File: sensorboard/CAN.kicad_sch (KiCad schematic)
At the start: 14 parts

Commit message: schemtiac update
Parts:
- JP11: renamed from JP?; footprint (none) -> Jumper:SolderJumper-2_P1.3mm_Open_RoundedPad1.0x1.5mm
- gave numbers to parts that had none: 13
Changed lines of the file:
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@@
   (symbol (lib_id "power:GND") (at 133.35 99.06 0) (unit 1)
     (in_bom yes) (on_board yes)
-    (property "Reference" "#PWR?" (id 0) (at 133.35 105.41 0)
+    (property "Reference" "#PWR0156" (id 0) (at 133.35 105.41 0)
       (effects (font (size 1.27 1.27)) hide)
     )
@@
   (symbol (lib_id "power:GND") (at 133.35 85.09 0) (unit 1)
     (in_bom yes) (on_board yes) (fields_autoplaced)
-    (property "Reference" "#PWR?" (id 0) (at 133.35 91.44 0)
+    (property "Reference" "#PWR0155" (id 0) (at 133.35 91.44 0)
       (effects (font (size 1.27 1.27)) hide)
     )
@@
   (symbol (lib_id "Device:C_Small") (at 87.63 83.82 180) (unit 1)
     (in_bom yes) (on_board yes)
-    (property "Reference" "C?" (id 0) (at 88.9 77.47 0)
+    (property "Reference" "C31" (id 0) (at 88.9 77.47 0)
       (effects (font (size 1.27 1.27)) (justify right))
     )
@@
   (symbol (lib_id "Device:C_Small") (at 133.35 96.52 180) (unit 1)
     (in_bom yes) (on_board yes)
-    (property "Reference" "C?" (id 0) (at 135.89 96.52 0)
+    (property "Reference" "C75" (id 0) (at 135.89 96.52 0)
       (effects (font (size 1.27 1.27)) (justify right))
     )
@@
   (symbol (lib_id "Interface_CAN_LIN:SN65HVD230") (at 104.14 83.82 0) (unit 1)
     (in_bom yes) (on_board yes)
-    (property "Reference" "U?" (id 0) (at 111.76 71.3486 0))
+    (property "Reference" "U20" (id 0) (at 111.76 71.3486 0))
     (property "Value" "SN65HVD230" (id 1) (at 111.76 73.66 0))
     (property "Footprint" "Package_SO:SOIC-8_3.9x4.9mm_P1.27mm" (id 2) (at 104.14 96.52 0)
@@
   (symbol (lib_id "Device:C") (at 129.54 85.09 90) (unit 1)
     (in_bom yes) (on_board yes)
-    (property "Reference" "C?" (id 0) (at 129.54 78.74 90))
+    (property "Reference" "C73" (id 0) (at 129.54 78.74 90))
     (property "Value" "0.1uF" (id 1) (at 129.54 81.28 90))
     (property "Footprint" "Capacitor_SMD:C_0603_1608Metric" (id 2) (at 133.35 84.1248 0)
@@
   (symbol (lib_id "Device:R_Small") (at 93.98 91.44 0) (unit 1)
     (in_bom yes) (on_board yes)
-    (property "Reference" "R?" (id 0) (at 90.17 96.52 0)
+    (property "Reference" "R69" (id 0) (at 90.17 96.52 0)
       (effects (font (size 1.27 1.27)) (justify left))
     )
@@
   (symbol (lib_id "Device:C_Small") (at 93.98 67.31 0) (unit 1)
     (in_bom yes) (on_board yes)
-    (property "Reference" "C?" (id 0) (at 86.36 66.04 0)
+    (property "Reference" "C71" (id 0) (at 86.36 66.04 0)
       (effects (font (size 1.27 1.27)) (justify left))
     )
@@
   (symbol (lib_id "Device:R") (at 125.73 80.01 0) (unit 1)
     (in_bom yes) (on_board yes)
-    (property "Reference" "R?" (id 0) (at 120.65 78.74 0)
+    (property "Reference" "R70" (id 0) (at 120.65 78.74 0)
       (effects (font (size 1.27 1.27)) (justify left))
     )
@@
   (symbol (lib_id "Device:R_Small") (at 83.82 81.28 90) (unit 1)
     (in_bom yes) (on_board yes)
-    (property "Reference" "R?" (id 0) (at 83.82 76.2 90))
+    (property "Reference" "R67" (id 0) (at 83.82 76.2 90))
     (property "Value" "90" (id 1) (at 83.82 78.74 90))
     (property "Footprint" "Resistor_SMD:R_0603_1608Metric" (id 2) (at 83.82 81.28 0)
@@
   (symbol (lib_id "power:GND") (at 96.52 69.85 0) (unit 1)
     (in_bom yes) (on_board yes)
-    (property "Reference" "#PWR?" (id 0) (at 96.52 76.2 0)
+    (property "Reference" "#PWR0153" (id 0) (at 96.52 76.2 0)
       (effects (font (size 1.27 1.27)) hide)
     )
@@
   (symbol (lib_id "Device:R_Small") (at 83.82 83.82 90) (unit 1)
     (in_bom yes) (on_board yes)
-    (property "Reference" "R?" (id 0) (at 83.82 86.36 90))
+    (property "Reference" "R68" (id 0) (at 83.82 86.36 90))
     (property "Value" "90" (id 1) (at 83.82 88.9 90))
     (property "Footprint" "Resistor_SMD:R_0603_1608Metric" (id 2) (at 83.82 83.82 0)
@@
   (symbol (lib_id "Diode:SM712_SOT23") (at 144.78 85.09 270) (unit 1)
     (in_bom yes) (on_board yes)
-    (property "Reference" "D?" (id 0) (at 148.59 83.82 90)
+    (property "Reference" "D8" (id 0) (at 148.59 83.82 90)
       (effects (font (size 1.27 1.27)) (justify left))
     )
@@
   (symbol (lib_id "Device:C_Small") (at 133.35 78.74 180) (unit 1)
     (in_bom yes) (on_board yes)
-    (property "Reference" "C?" (id 0) (at 124.46 71.12 0)
+    (property "Reference" "C74" (id 0) (at 124.46 71.12 0)
       (effects (font (size 1.27 1.27)) (justify right))
     )
@@
   (symbol (lib_id "power:GND") (at 104.14 95.25 0) (unit 1)
     (in_bom yes) (on_board yes)
-    (property "Reference" "#PWR?" (id 0) (at 104.14 101.6 0)
+    (property "Reference" "#PWR0154" (id 0) (at 104.14 101.6 0)
       (effects (font (size 1.27 1.27)) hide)
     )
@@
   (symbol (lib_id "Jumper:SolderJumper_2_Open") (at 119.38 85.09 0) (unit 1)
     (in_bom yes) (on_board yes) (fields_autoplaced)
-    (property "Reference" "JP?" (id 0) (at 119.38 78.74 0))
+    (property "Reference" "JP11" (id 0) (at 119.38 78.74 0))
     (property "Value" "SolderJumper_2_Open" (id 1) (at 119.38 81.28 0))
-    (property "Footprint" "" (id 2) (at 119.38 85.09 0)
+    (property "Footprint" "Jumper:SolderJumper-2_P1.3mm_Open_RoundedPad1.0x1.5mm" (id 2) (at 119.38 85.09 0)
       (effects (font (size 1.27 1.27)) hide)
     )
@@
   (symbol (lib_id "Device:C_Small") (at 99.06 67.31 0) (unit 1)
     (in_bom yes) (on_board yes) (fields_autoplaced)
-    (property "Reference" "C?" (id 0) (at 101.6 66.0462 0)
+    (property "Reference" "C72" (id 0) (at 101.6 66.0462 0)
       (effects (font (size 1.27 1.27)) (justify left))
     )
@@
   (symbol (lib_id "power:+3.3V") (at 96.52 64.77 0) (unit 1)
     (in_bom yes) (on_board yes)
-    (property "Reference" "#PWR?" (id 0) (at 96.52 68.58 0)
+    (property "Reference" "#PWR0152" (id 0) (at 96.52 68.58 0)
       (effects (font (size 1.27 1.27)) hide)
     )
@@
   (symbol (lib_id "Device:R") (at 125.73 90.17 0) (unit 1)
     (in_bom yes) (on_board yes)
-    (property "Reference" "R?" (id 0) (at 120.65 88.9 0)
-      (effects (font (size 1.27 1.27)) (justify left))
-    )
+    (property "Reference" "R71" (id 0) (at 120.65 88.9 0)
+      (effects (font (size 1.27 1.27)) (justify left))
+    )

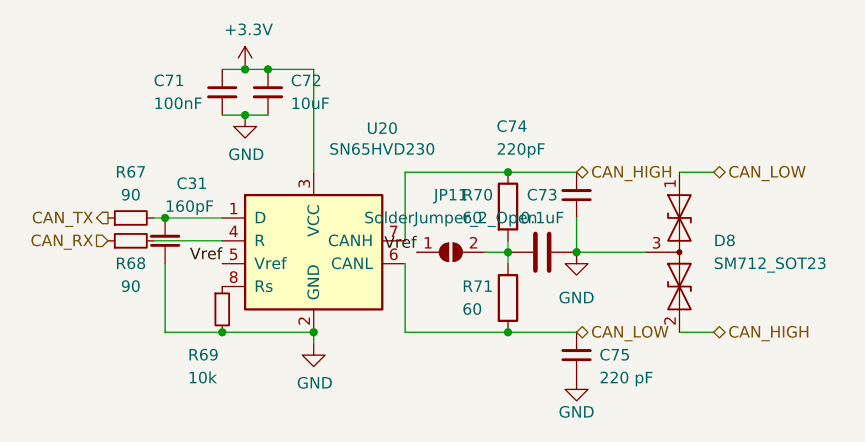
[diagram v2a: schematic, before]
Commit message: changed BOOT pin, auto reset caps
moved references about
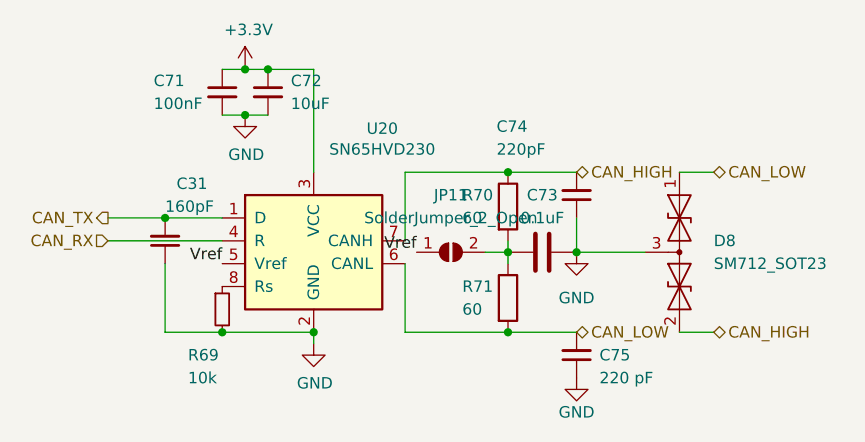
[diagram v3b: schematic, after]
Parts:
- removed R67, R68: 90, Resistor_SMD:R_0603_1608Metric, symbol Device:R_Small
- R70, R71: footprint Resistor_SMD:R_0805_2012Metric -> Resistor_SMD:R_0603_1608Metric
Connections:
- net CAN_RX: now also U20.4 (R)
- net CAN_TX: now also C31.2, U20.1 (D)
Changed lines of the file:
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@@
   (junction (at 125.73 85.09) (diameter 0) (color 0 0 0 0)
   )
-  (wire (pts (xy 86.36 81.28) (xy 87.63 81.28))
+  (wire (pts (xy 81.28 81.28) (xy 87.63 81.28))
     (stroke (width 0) (type default) (color 0 0 0 0))
   )
@@
     (stroke (width 0) (type default) (color 0 0 0 0))
   )
-  (wire (pts (xy 86.36 83.82) (xy 93.98 83.82))
+  (wire (pts (xy 81.28 83.82) (xy 93.98 83.82))
     (stroke (width 0) (type default) (color 0 0 0 0))
   )
@@
       (effects (font (size 1.27 1.27)) (justify left))
     )
-    (property "Footprint" "Resistor_SMD:R_0805_2012Metric" (id 2) (at 123.952 80.01 90)
+    (property "Footprint" "Resistor_SMD:R_0603_1608Metric" (id 2) (at 123.952 80.01 90)
       (effects (font (size 1.27 1.27)) hide)
     )
     (property "Datasheet" "~" (id 3) (at 125.73 80.01 0)
-      (effects (font (size 1.27 1.27)) hide)
-    )
-    (pin "1")
-    (pin "2")
-  )
-  (symbol (lib_id "Device:R_Small") (at 83.82 81.28 90) (unit 1)
-    (in_bom yes) (on_board yes)
-    (property "Reference" "R67" (id 0) (at 83.82 76.2 90))
-    (property "Value" "90" (id 1) (at 83.82 78.74 90))
-    (property "Footprint" "Resistor_SMD:R_0603_1608Metric" (id 2) (at 83.82 81.28 0)
-      (effects (font (size 1.27 1.27)) hide)
-    )
-    (property "Datasheet" "~" (id 3) (at 83.82 81.28 0)
       (effects (font (size 1.27 1.27)) hide)
     )
@@
     )
     (pin "1")
-  )
-  (symbol (lib_id "Device:R_Small") (at 83.82 83.82 90) (unit 1)
-    (in_bom yes) (on_board yes)
-    (property "Reference" "R68" (id 0) (at 83.82 86.36 90))
-    (property "Value" "90" (id 1) (at 83.82 88.9 90))
-    (property "Footprint" "Resistor_SMD:R_0603_1608Metric" (id 2) (at 83.82 83.82 0)
-      (effects (font (size 1.27 1.27)) hide)
-    )
-    (property "Datasheet" "~" (id 3) (at 83.82 83.82 0)
-      (effects (font (size 1.27 1.27)) hide)
-    )
-    (pin "1")
-    (pin "2")
   )
   (symbol (lib_id "Diode:SM712_SOT23") (at 144.78 85.09 270) (unit 1)
@@
       (effects (font (size 1.27 1.27)) (justify left))
     )
-    (property "Footprint" "Resistor_SMD:R_0805_2012Metric" (id 2) (at 123.952 90.17 90)
-      (effects (font (size 1.27 1.27)) hide)
-    )
+    (property "Footprint" "Resistor_SMD:R_0603_1608Metric" (id 2) (at 123.952 90.17 90)
+      (effects (font (size 1.27 1.27)) hide)
+    )
